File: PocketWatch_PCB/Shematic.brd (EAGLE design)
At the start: 53 x 56 mm, 52 parts, among them IC1 74HC139D, Q1 BCX71SMD, Q2 BCX71SMD, Q3 BCX71SMD, Q4 BCX71SMD, U2 ATTINY88-AU

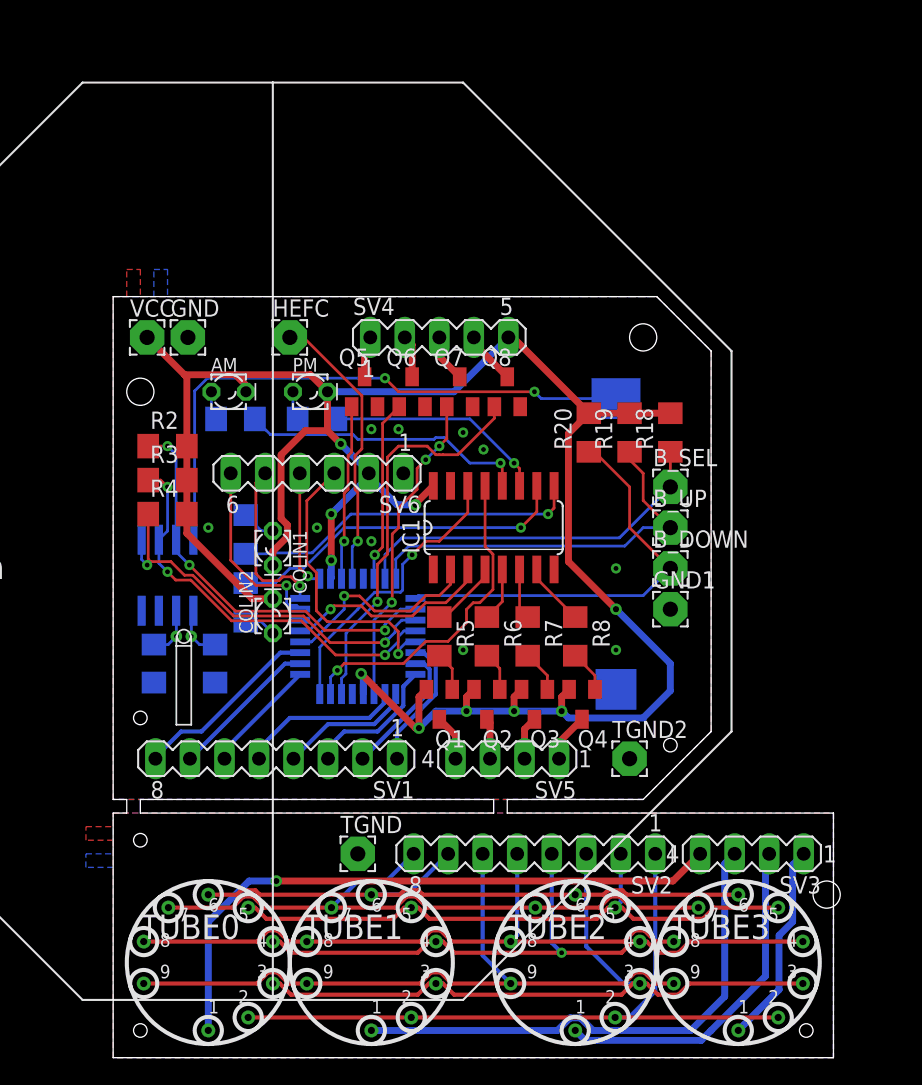
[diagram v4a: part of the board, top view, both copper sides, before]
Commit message: Rearranged bottom board to be much more thin.
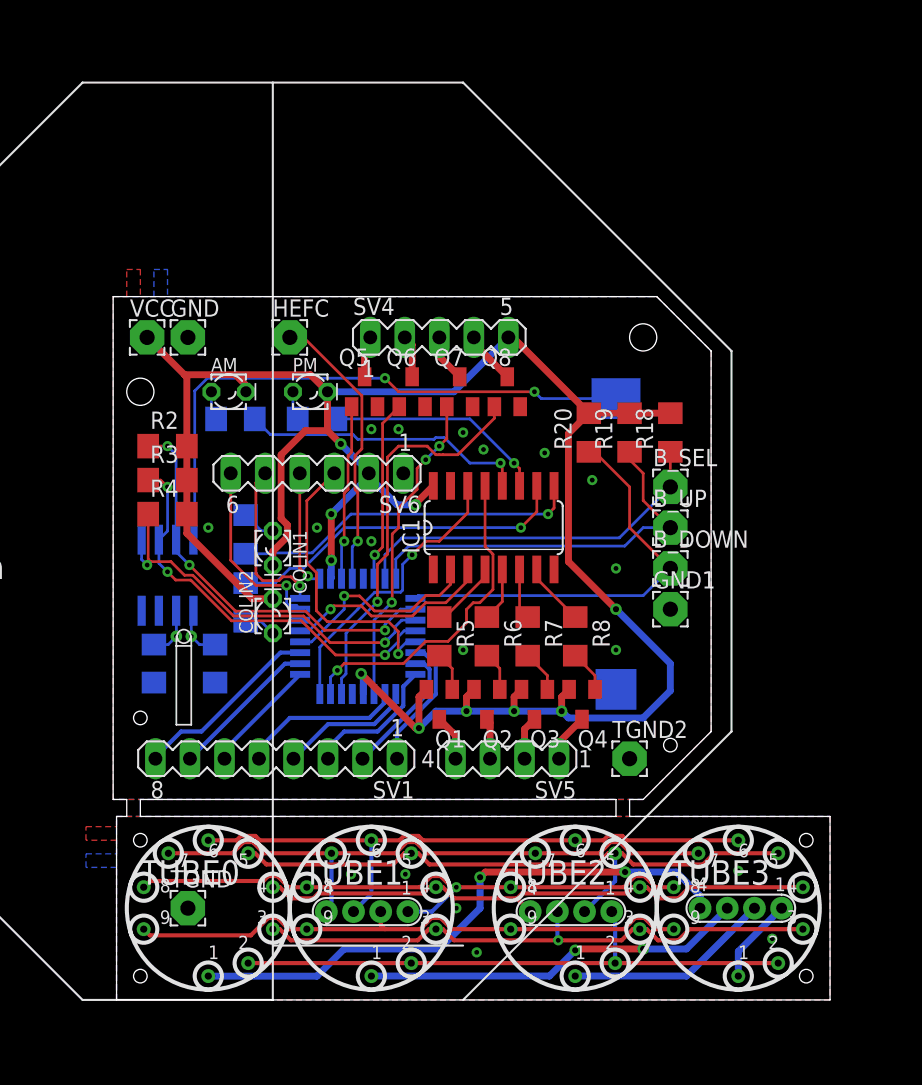
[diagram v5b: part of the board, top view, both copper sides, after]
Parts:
- added SV7: H04, Library:H04
- SV2: value (none) -> H04; device con-lstb:MA08-1 -> Library:H04
- SV3: value (none) -> H04; device con-lstb:MA04-1 -> Library:H04
- moved TGND 13.1 mm to (5.50, 11.0)
- moved SV2 13.0 mm to (18.8, 10.8), turned to 0 degrees
- moved SV3 4.07 mm to (46.2, 11.0), turned to 0 degrees
- moved TUBE0 4.00 mm to (7.00, 11.0)
- moved TUBE1 4.00 mm to (19.0, 11.0)
- moved TUBE2 4.00 mm to (34.0, 11.0)
- moved TUBE3 4.00 mm to (46.0, 11.0)
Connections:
- net SEG_A_2: now also SV7.2; no longer SV2.2
- net SEG_B_2: now also SV7.3; no longer SV2.3
- net SEG_C_2: now also SV7.4; no longer SV2.4
- net SEG_DOT_2: now also SV7.1; no longer SV2.1
- net SEG_D_2: now also SV2.1; no longer SV2.5
- net SEG_E_2: now also SV2.2; no longer SV2.6
- net SEG_F_2: now also SV2.3; no longer SV2.7
- net SEG_G_2: now also SV2.4; no longer SV2.8
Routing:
- net T1_2: track 38.6 -> 28.3 mm, vias 0 -> 2
- net T2_2: track 25.4 -> 15.3 mm
- net SEG_DOT_2: track 52.9 -> 42.9 mm
- net SEG_B_2: track 52.9 -> 43.2 mm, vias 0 -> 1
- net T3_2: track 15.0 -> 6.31 mm
- net SEG_E_2: track 51.4 -> 42.8 mm
- net SEG_C_2: track 48.6 -> 42.4 mm, vias 1 -> 0
- net T0_2: track 46.3 -> 42.3 mm, vias 1 -> 2
- net SEG_G_2: track 48.7 -> 45.5 mm
- net SEG_D_2: track 47.7 -> 45.3 mm, vias 0 -> 1
- net SEG_F_2: track 46.7 -> 45.6 mm
- net SEG_A_2: track 45.2 -> 46.3 mm
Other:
- board size 53 x 56 mm -> 52.8 x 51.8 mm

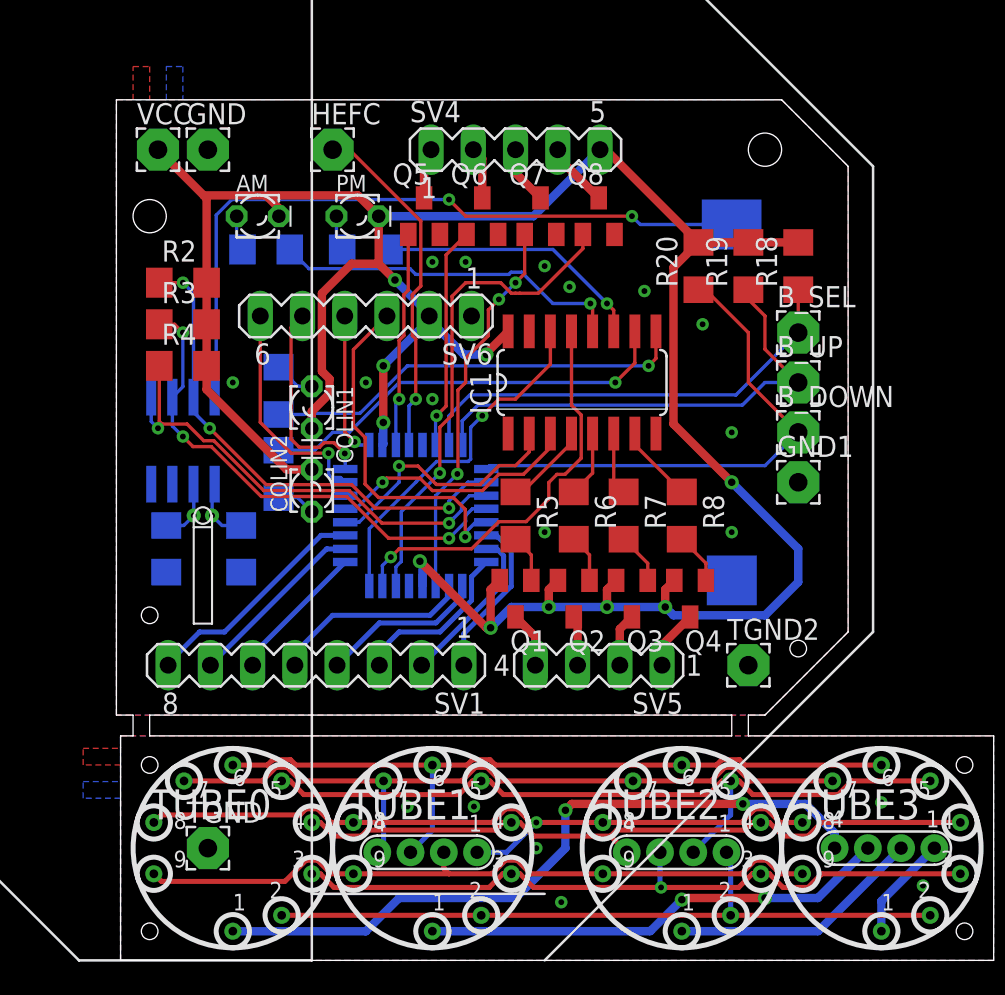
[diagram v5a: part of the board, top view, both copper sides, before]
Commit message: Miscellaneous adjustments and ground plane fixes
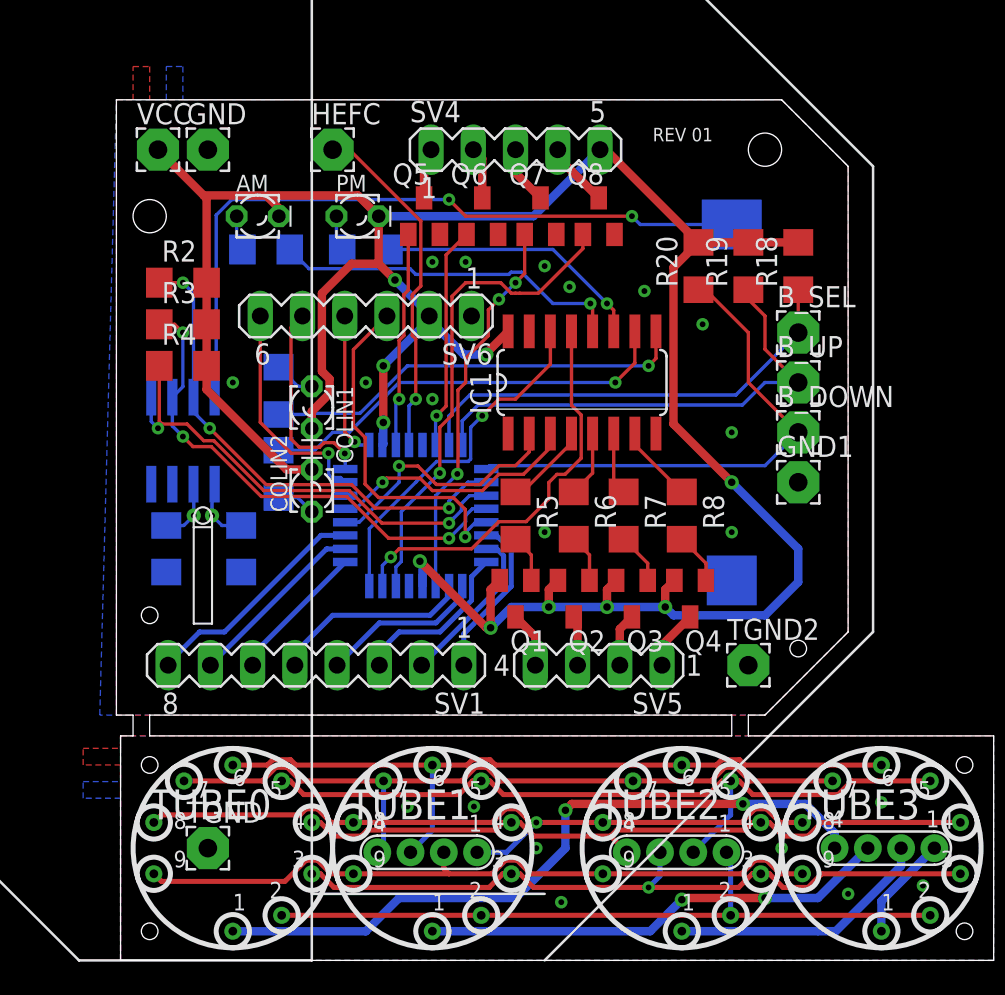
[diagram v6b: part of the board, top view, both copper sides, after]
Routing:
- net T2_2: track 15.3 -> 15.9 mm
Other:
- board text added: "REV 01"
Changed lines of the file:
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@@
 <hole x="51" y="6" drill="1"/>
 <hole x="51" y="16" drill="1"/>
+<text x="32.25" y="53.5" size="0.8128" layer="21">REV 01</text>
 </plain>
 <attributes>
@@
 <contactref element="Q6" pad="2"/>
 <contactref element="GND1" pad="1"/>
-<polygon width="0.2032" layer="1" isolate="0.254">
+<polygon width="0.2032" layer="1" isolate="0.254" rank="2">
 <vertex x="1" y="58"/>
 <vertex x="2" y="58"/>
@@
 <vertex x="1" y="56"/>
 </polygon>
-<polygon width="0.2032" layer="16" isolate="0.254">
+<polygon width="0.2032" layer="16" isolate="0.254" rank="2">
 <vertex x="3" y="58"/>
 <vertex x="4" y="58"/>
@@
 <vertex x="44" y="24"/>
 <vertex x="39" y="19"/>
-<vertex x="0" y="19"/>
+<vertex x="-1" y="19"/>
 <vertex x="0" y="56"/>
 <vertex x="3" y="56"/>
@@
 <wire x1="38.2350875" y1="9.4566" x2="38.75" y2="9.4566" width="0.3048" layer="1"/>
 <wire x1="24.2649125" y1="9.4566" x2="25.0862125" y2="8.6353" width="0.3048" layer="1"/>
-<wire x1="25.0862125" y1="8.6353" x2="32.75" y2="8.6353" width="0.3048" layer="1"/>
-<wire x1="32.75" y1="8.6353" x2="37.4137875" y2="8.6353" width="0.3048" layer="1"/>
+<wire x1="25.0862125" y1="8.6353" x2="32" y2="8.6353" width="0.3048" layer="1"/>
+<wire x1="32" y1="8.6353" x2="37.4137875" y2="8.6353" width="0.3048" layer="1"/>
 <wire x1="37.4137875" y1="8.6353" x2="38.2350875" y2="9.4566" width="0.3048" layer="1"/>
 <wire x1="38.75" y1="9.4566" x2="39.2649125" y2="9.4566" width="0.3048" layer="1"/>
@@
 <wire x1="40.0862125" y1="8.6353" x2="41.59019375" y2="8.6353" width="0.3048" layer="1"/>
 <contactref element="SV7" pad="3"/>
-<wire x1="32.686" y1="10.75" x2="32.686" y2="8.6993" width="0.3048" layer="16"/>
-<wire x1="32.686" y1="8.6993" x2="32.75" y2="8.6353" width="0.3048" layer="16"/>
-<via x="32.75" y="8.6353" extent="1-16" drill="0.35"/>
+<wire x1="32.686" y1="10.75" x2="32.686" y2="9.3213" width="0.3048" layer="16"/>
+<wire x1="32.686" y1="9.3213" x2="32" y2="8.6353" width="0.3048" layer="16"/>
+<via x="32" y="8.6353" extent="1-16" drill="0.35"/>
 </signal>
 <signal name="SEG_C_2">
@@
 <contactref element="TUBE2" pad="1"/>
 <contactref element="SV3" pad="2"/>
-<wire x1="47.186" y1="11" x2="42.1916" y2="6.0056" width="0.508" layer="16"/>
-<wire x1="42.1916" y1="6.0056" x2="34" y2="6.0056" width="0.508" layer="16"/>
+<wire x1="34" y1="6.0056" x2="42.1916" y2="6.0056" width="0.508" layer="16"/>
+<wire x1="43.2556" y1="6.0056" x2="42.1916" y2="6.0056" width="0.508" layer="16"/>
+<wire x1="47.186" y1="11" x2="47.186" y2="9.936" width="0.508" layer="16"/>
+<wire x1="47.186" y1="9.936" x2="43.2556" y2="6.0056" width="0.508" layer="16"/>
 </signal>
 <signal name="T3_2">
@@
 <via x="48.5" y="8.75" extent="1-16" drill="0.35"/>
 <via x="25.25" y="11" extent="1-16" drill="0.35"/>
+<via x="44" y="8.25" extent="1-16" drill="0.35"/>
+<via x="40" y="11" extent="1-16" drill="0.35"/>
 </signal>
 <signal name="N$8">

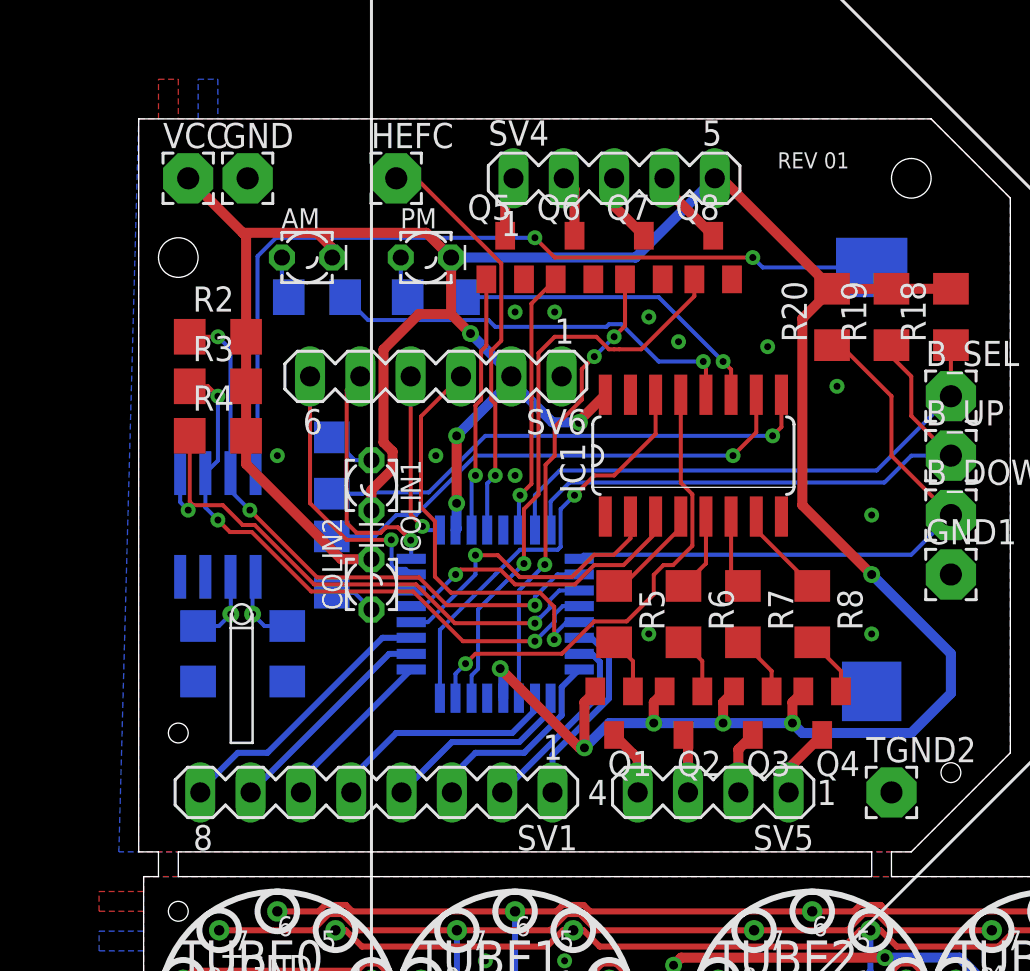
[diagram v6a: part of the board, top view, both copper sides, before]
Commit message: Added second version of the board for attempted board optimization
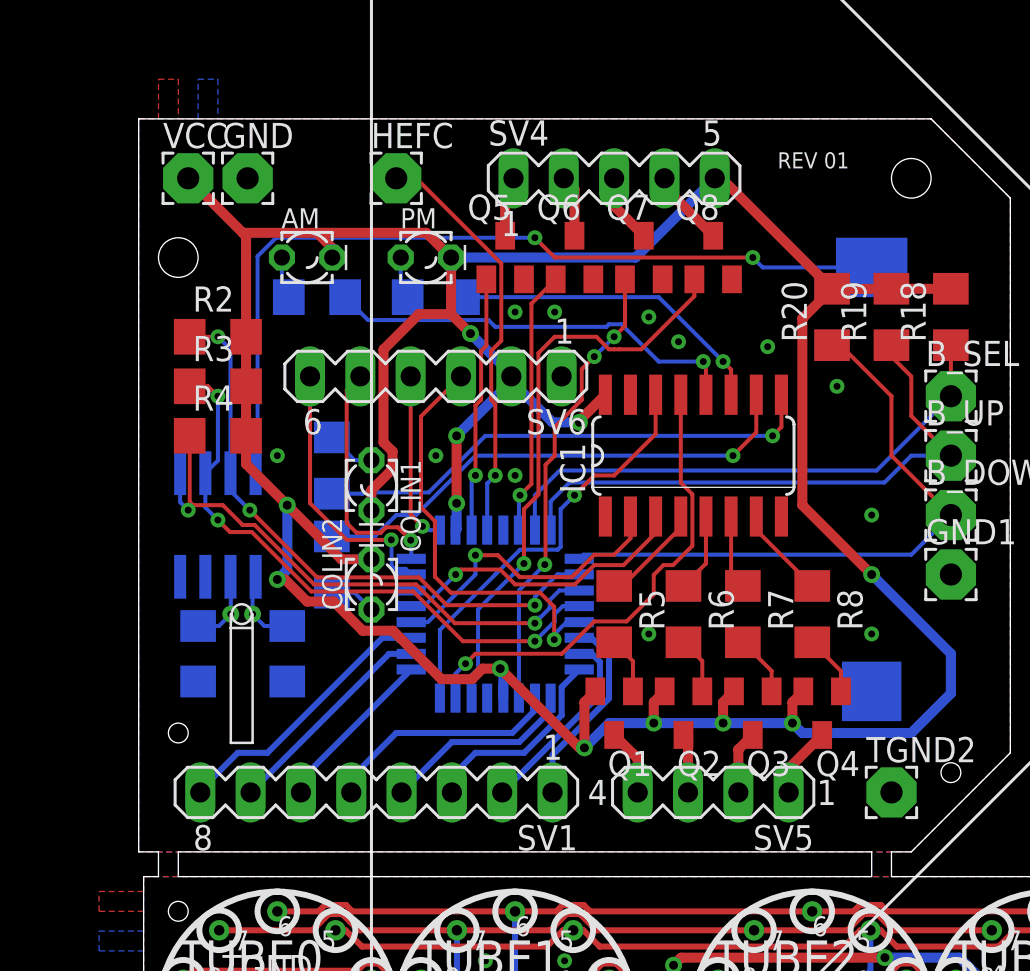
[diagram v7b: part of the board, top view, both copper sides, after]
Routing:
- net VCC: track 161.4 -> 178.9 mm, vias 10 -> 12
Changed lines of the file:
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@@
 <vertex x="44" y="24"/>
 <vertex x="39" y="19"/>
-<vertex x="-1" y="19"/>
+<vertex x="0" y="19"/>
 <vertex x="0" y="56"/>
 <vertex x="3" y="56"/>
@@
 <wire x1="11.75" y1="33.77" x2="10.23" y2="33.77" width="0.508" layer="1"/>
 <wire x1="5.422" y1="38.578" x2="5.422" y2="40" width="0.508" layer="1"/>
-<wire x1="10.23" y1="33.77" x2="5.422" y2="38.578" width="0.508" layer="1"/>
+<wire x1="10.23" y1="33.77" x2="7.5" y2="36.5" width="0.508" layer="1"/>
+<wire x1="7.5" y1="36.5" x2="5.422" y2="38.578" width="0.508" layer="1"/>
 <wire x1="26.55" y1="27.1" x2="26" y2="26.55" width="0.508" layer="1"/>
 <wire x1="26" y1="26.55" x2="26" y2="25.5" width="0.508" layer="1"/>
@@
 <wire x1="33.5" y1="45.922" x2="35" y2="47.422" width="0.508" layer="1"/>
 <wire x1="33.5" y1="36.5" x2="33.5" y2="45.922" width="0.508" layer="1"/>
+<via x="7.5" y="36.5" extent="1-16" drill="0.45"/>
+<wire x1="7.5" y1="36.5" x2="7.5" y2="33.25" width="0.508" layer="16"/>
+<wire x1="7.5" y1="33.25" x2="7" y2="32.75" width="0.508" layer="16"/>
+<via x="7" y="32.75" extent="1-16" drill="0.45"/>
+<wire x1="18.25" y1="28.25" x2="17.35959375" y2="28.25" width="0.508" layer="1"/>
+<wire x1="17.35959375" y1="28.25" x2="16.82499375" y2="27.7154" width="0.508" layer="1"/>
+<wire x1="16.82499375" y1="27.7154" x2="15.2846" y2="27.7154" width="0.508" layer="1"/>
+<wire x1="12.8368" y1="30.1632" x2="11.3081125" y2="30.1632" width="0.508" layer="1"/>
+<wire x1="11.3081125" y1="30.1632" x2="9.8349125" y2="31.6364" width="0.508" layer="1"/>
+<wire x1="15.2846" y1="27.7154" x2="12.8368" y2="30.1632" width="0.508" layer="1"/>
+<wire x1="7.38689375" y1="32.75" x2="7" y2="32.75" width="0.508" layer="1"/>
+<wire x1="8.50049375" y1="31.6364" x2="7.38689375" y2="32.75" width="0.508" layer="1"/>
+<wire x1="9.8349125" y1="31.6364" x2="8.50049375" y2="31.6364" width="0.508" layer="1"/>
 </signal>
 <signal name="MOSI">
